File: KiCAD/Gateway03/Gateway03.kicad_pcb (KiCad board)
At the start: 2 copper layers, 54 x 54 mm, 8 parts, among them U1 LSHM, U2 LSHM, U3 LSHM, U4 LSHM, U5 LSHM, U6 LSHM, U7 LSHM, U8 LSHM

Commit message: finished Gateway03
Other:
- board size 54 x 54 mm -> 53 x 53 mm
- board text added: "Nov 2019"
- board text removed: "Oct 2019"

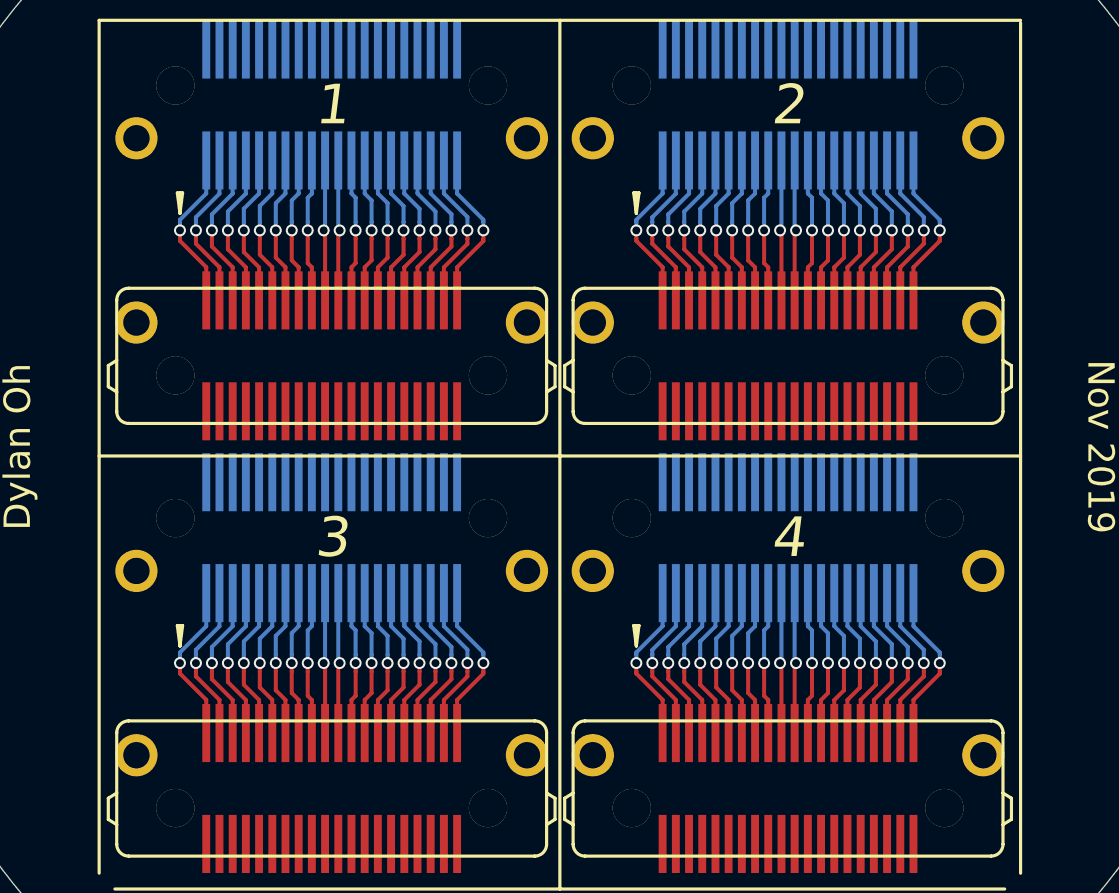
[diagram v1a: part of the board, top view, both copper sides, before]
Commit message: fixed via spacing issue on Gateway03
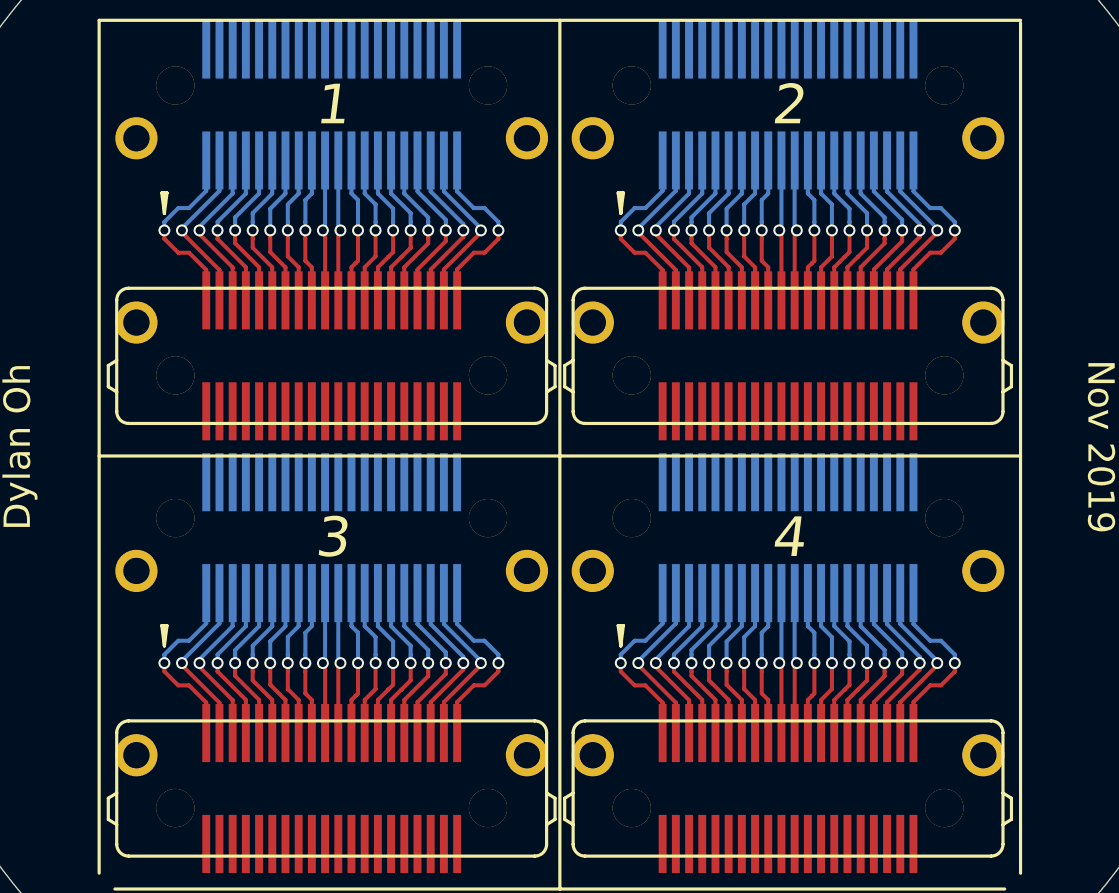
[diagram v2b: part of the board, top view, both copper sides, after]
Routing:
- net Net-(U5-Pad10): track 7.32 -> 6.05 mm
- net Net-(U5-Pad32): track 7.32 -> 6.05 mm
- net Net-(U5-Pad34): track 7.27 -> 6.19 mm
- net Net-(U5-Pad8): track 7.27 -> 6.19 mm
- net Net-(U5-Pad40): track 7.12 -> 8.09 mm
- net Net-(U3-Pad40): track 6.12 -> 7.09 mm
- net Net-(U7-Pad40): track 6.12 -> 7.09 mm
- net Net-(U1-Pad40): track 6.12 -> 7.09 mm
- net Net-(U7-Pad2): track 6.12 -> 7.07 mm
- net Net-(U3-Pad2): track 6.12 -> 7.07 mm
- net Net-(U5-Pad2): track 7.12 -> 8.07 mm
- net Net-(U1-Pad2): track 6.12 -> 7.07 mm
- net Net-(U5-Pad6): track 7.22 -> 6.32 mm
- net Net-(U5-Pad36): track 7.22 -> 6.34 mm
